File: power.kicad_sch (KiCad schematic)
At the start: 59 parts, among them J3 Conn_02x05_Odd_Even, T1 net-tie, U1 LMR54410, U11 RT9080-33GJ5, U3 TPS546D24ARVFR, U4 MIC5504

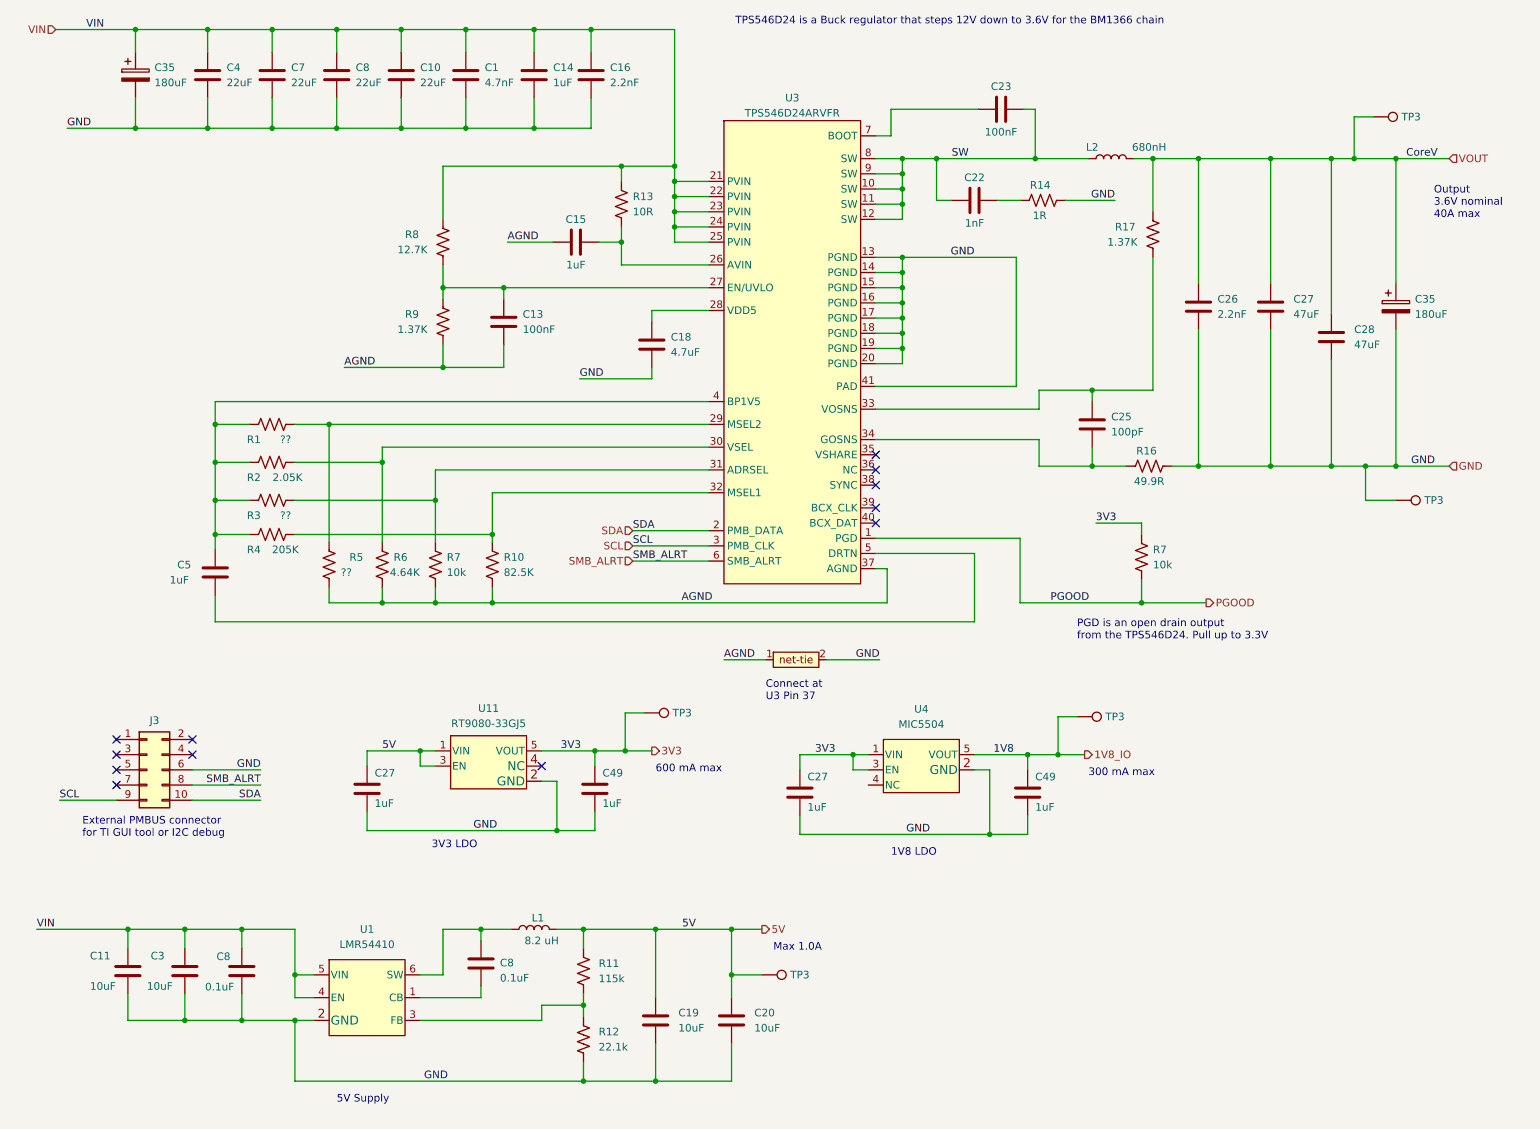
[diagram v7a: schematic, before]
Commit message: add PMBus isolation resistors
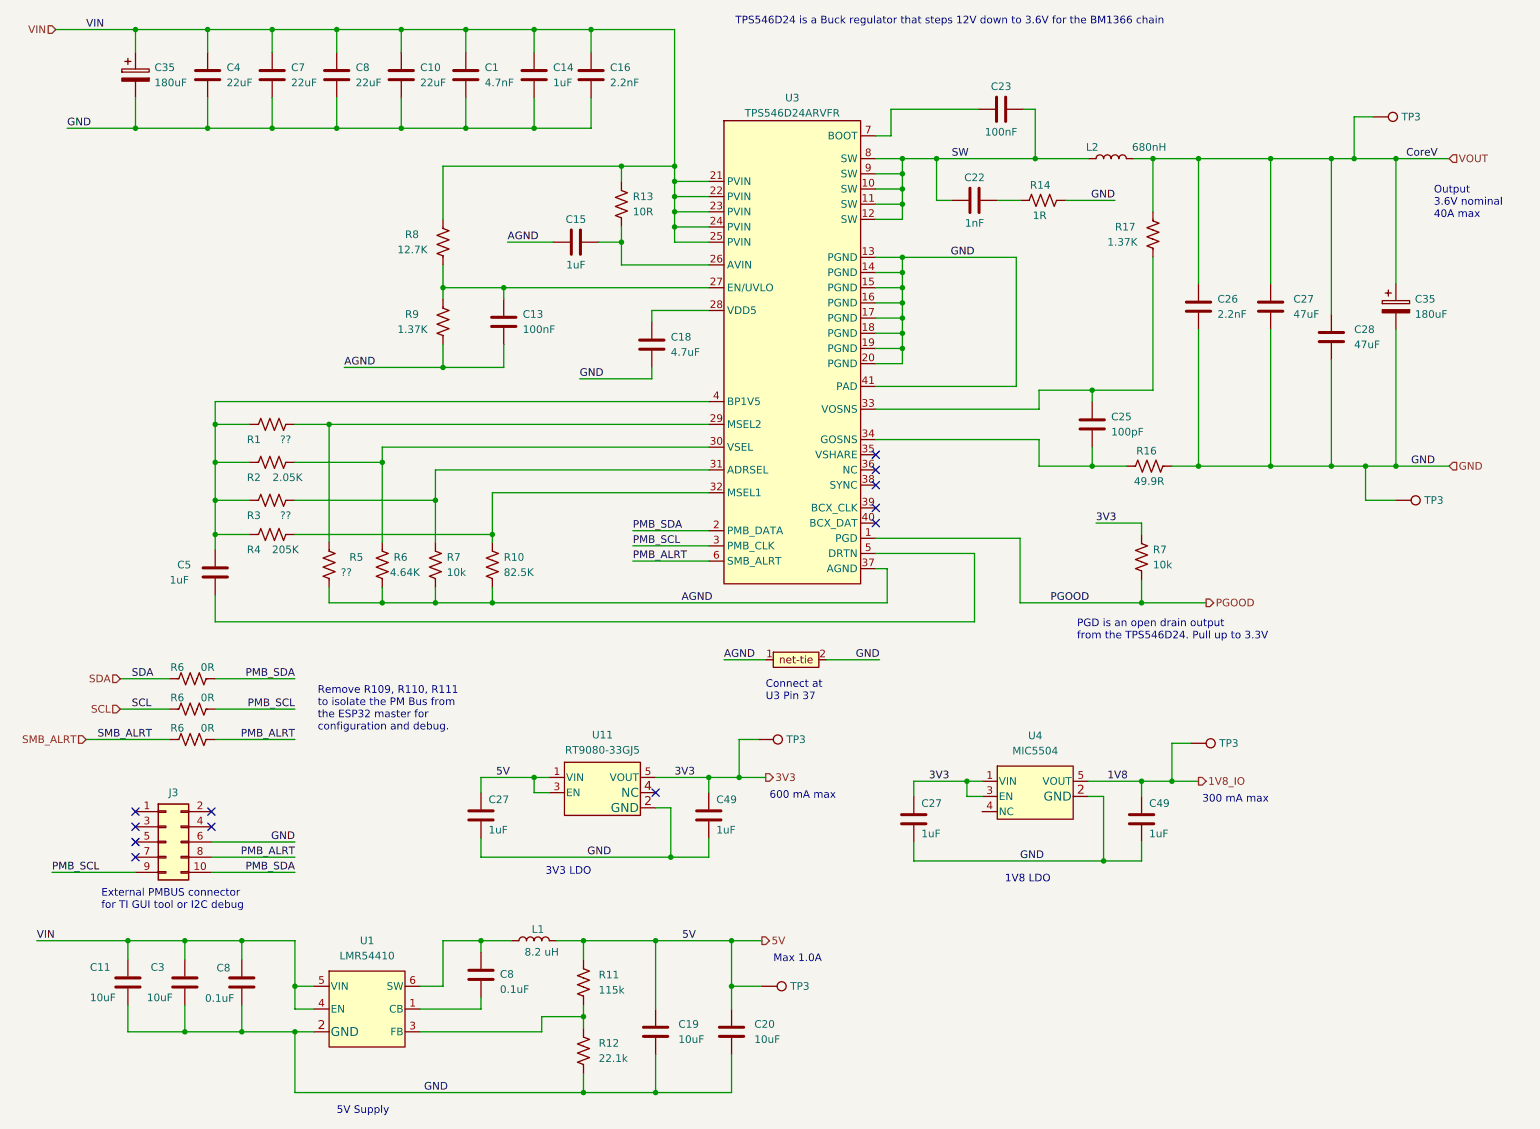
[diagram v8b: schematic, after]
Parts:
- added R6 (x3): 0R, Resistor_SMD:R_0402_1005Metric, symbol Device:R_US
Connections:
- net SCL: now also R6.1; no longer J3.9 (Pin_9), U3.3 (PMB_CLK)
- net SDA: now also R6.1; no longer J3.10 (Pin_10), U3.2 (PMB_DATA)
- net SMB_ALRT: now also R6.1; no longer J3.8 (Pin_8), U3.6 (SMB_ALRT)
- new net PMB_ALRT: J3.8 (Pin_8), R6.2, U3.6 (SMB_ALRT)
- new net PMB_SCL: J3.9 (Pin_9), R6.2, U3.3 (PMB_CLK)
- new net PMB_SDA: J3.10 (Pin_10), R6.2, U3.2 (PMB_DATA)
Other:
- note added: "Remove R109, R110, R111 to isolate the PM Bus from the ESP32 master for configuration and debug."
- moved on the sheet: C11, C19, C20, C27, C3, C49, C8, J3, L1, R11, R12, TP3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
